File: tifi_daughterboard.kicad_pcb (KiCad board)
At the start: 2 copper layers, 57.4 x 32.3 mm, 26 parts, among them J1 SSW-110-23-F-D, J2 SSW-110-23-F-D, J3 SM04B-SRSS-TB(LF)(SN), J4 SSW-103-02-T-S-RA, J5 PH2-04-UA, Q1 BSS138LT1G, U1 SGP40-D-R4, U2 SHT40-AD1B-R3

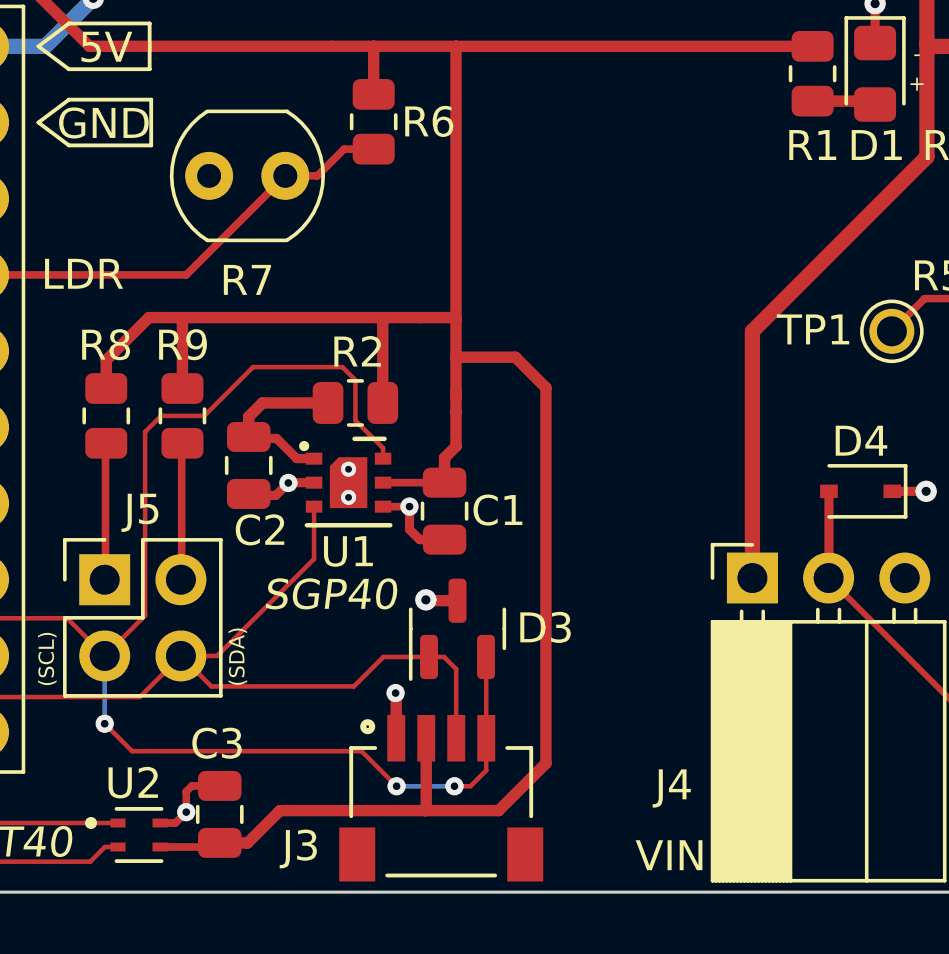
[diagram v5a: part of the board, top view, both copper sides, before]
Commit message: Add bulk capacitors to schmatic and board.
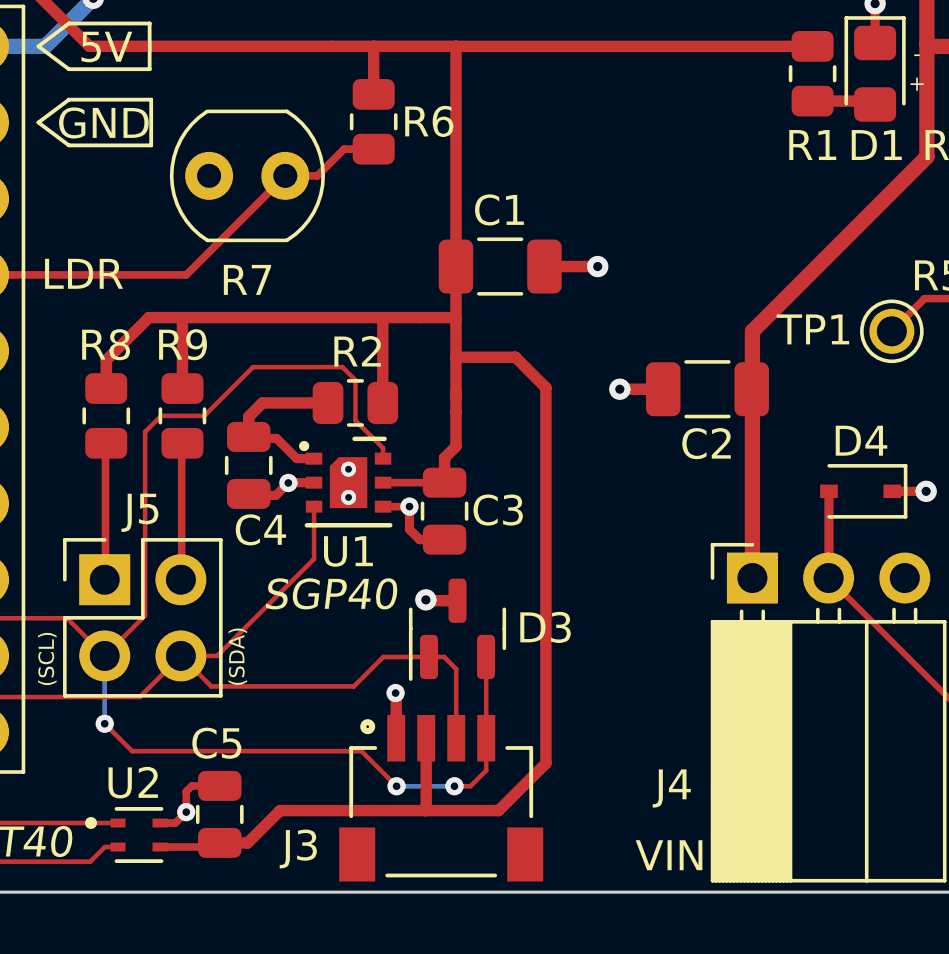
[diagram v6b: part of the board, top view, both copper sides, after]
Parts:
- added C1: 22uF, Capacitor_SMD:C_1206_3216Metric, F.Cu at (141.7, 81.0)
- added C2: 22uF, Capacitor_SMD:C_1206_3216Metric, F.Cu at (148.6, 85.1)
- renumbered C1 to C3, C2 to C4, C3 to C5
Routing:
- net GND: track 15.6 -> 18.8 mm, vias 11 -> 13
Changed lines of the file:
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@@
   (net 41 "unconnected-(J2-Pad20)")
   (net 42 "Net-(Q1-Pad2)")
-  (net 43 "Net-(C2-Pad1)")
+  (net 43 "Net-(R2-Pad2)")
   (net 44 "unconnected-(J1-Pad9)")
   (net 45 "Net-(J5-Pad1)")
@@
       (net 1 "+3.3V") (pintype "passive"))
     (pad "2" smd roundrect (at 0.9125 0 180) (size 1.025 1.4) (layers "F.Cu" "F.Paste" "F.Mask") (roundrect_rratio 0.243902439)
-      (net 43 "Net-(C2-Pad1)") (pintype "passive"))
+      (net 43 "Net-(R2-Pad2)") (pintype "passive"))
     (model "${KICAD6_3DMODEL_DIR}/Resistor_SMD.3dshapes/R_0805_2012Metric.wrl"
       (offset (xyz 0 0 0))
@@
     (property "Sheetname" "")
     (attr smd)
-    (fp_text reference "C2" (at 2.1844 -0.4064 180) (layer "F.SilkS")
+    (fp_text reference "C4" (at 2.1844 -0.4064 180) (layer "F.SilkS")
       (effects (font (size 1 1) (thickness 0.15)))
     )
@@
     (fp_line (start -1 0.625) (end -1 -0.625) (layer "F.Fab") (width 0.1))
     (pad "1" smd roundrect (at -0.95 0 270) (size 1 1.45) (layers "F.Cu" "F.Paste" "F.Mask") (roundrect_rratio 0.25)
-      (net 43 "Net-(C2-Pad1)") (pintype "passive"))
+      (net 43 "Net-(R2-Pad2)") (pintype "passive"))
     (pad "2" smd roundrect (at 0.95 0 270) (size 1 1.45) (layers "F.Cu" "F.Paste" "F.Mask") (roundrect_rratio 0.25)
       (net 2 "GND") (pintype "passive"))
@@
     )
   )
+  (footprint "Capacitor_SMD:C_1206_3216Metric" (layer "F.Cu")
+    (at 148.59 85.09 180)
+    (descr "Capacitor SMD 1206 (3216 Metric), square (rectangular) end terminal, IPC_7351 nominal, (Body size source: IPC-SM-782 page 76, https://www.pcb-3d.com/wordpress/wp-content/uploads/ipc-sm-782a_amendment_1_and_2.pdf), generated with kicad-footprint-generator")
+    (tags "capacitor")
+    (property "Sheetfile" "tifi_daughterboard.kicad_sch")
+    (property "Sheetname" "")
+    (property "Supplier Link" "https://www.digikey.com/en/products/detail/samsung-electro-mechanics/CL31B226MPHNNNE/3888806")
+    (attr smd)
+    (fp_text reference "C2" (at 0 -1.85) (layer "F.SilkS")
+      (effects (font (size 1 1) (thickness 0.15)))
+    )
+    (fp_text value "22uF" (at 0 1.85) (layer "F.Fab")
+      (effects (font (size 1 1) (thickness 0.15)))
+    )
+    (fp_text user "${REFERENCE}" (at 0 0) (layer "F.Fab")
+      (effects (font (size 0.8 0.8) (thickness 0.12)))
+    )
+    (fp_line (start -0.711252 0.91) (end 0.711252 0.91) (layer "F.SilkS") (width 0.12))
+    (fp_line (start -0.711252 -0.91) (end 0.711252 -0.91) (layer "F.SilkS") (width 0.12))
+    (fp_line (start -2.3 1.15) (end -2.3 -1.15) (layer "F.CrtYd") (width 0.05))
+    (fp_line (start 2.3 1.15) (end -2.3 1.15) (layer "F.CrtYd") (width 0.05))
+    (fp_line (start 2.3 -1.15) (end 2.3 1.15) (layer "F.CrtYd") (width 0.05))
+    (fp_line (start -2.3 -1.15) (end 2.3 -1.15) (layer "F.CrtYd") (width 0.05))
+    (fp_line (start 1.6 -0.8) (end 1.6 0.8) (layer "F.Fab") (width 0.1))
+    (fp_line (start -1.6 0.8) (end -1.6 -0.8) (layer "F.Fab") (width 0.1))
+    (fp_line (start -1.6 -0.8) (end 1.6 -0.8) (layer "F.Fab") (width 0.1))
+    (fp_line (start 1.6 0.8) (end -1.6 0.8) (layer "F.Fab") (width 0.1))
+    (pad "1" smd roundrect (at -1.475 0 180) (size 1.15 1.8) (layers "F.Cu" "F.Paste" "F.Mask") (roundrect_rratio 0.217391)
+      (net 6 "+5V") (pintype "passive"))
+    (pad "2" smd roundrect (at 1.475 0 180) (size 1.15 1.8) (layers "F.Cu" "F.Paste" "F.Mask") (roundrect_rratio 0.217391)
+      (net 2 "GND") (pintype "passive"))
+    (model "${KICAD6_3DMODEL_DIR}/Capacitor_SMD.3dshapes/C_1206_3216Metric.wrl"
+      (offset (xyz 0 0 0))
+      (scale (xyz 1 1 1))
+      (rotate (xyz 0 0 0))
+    )
+  )
   (footprint "LED_SMD:LED_0805_2012Metric_Pad1.15x1.40mm_HandSolder" (layer "F.Cu")
     (at 160.2486 74.5654 -90)
@@
     (property "Sheetfile" "tifi_daughterboard.kicad_sch")
     (property "Sheetname" "")
+    (property "Supplier Link" "https://www.digikey.com/en/products/detail/onsemi/BSS138LT1G/918376")
     (attr smd)
     (fp_text reference "Q1" (at 0 -2.7178 180) (layer "F.SilkS")
@@
     (property "Sheetname" "")
     (attr smd)
-    (fp_text reference "C3" (at 2.3368 -0.0762 180) (layer "F.SilkS")
+    (fp_text reference "C5" (at 2.3368 -0.0762 180) (layer "F.SilkS")
       (effects (font (size 1 1) (thickness 0.15)))
     )
@@
       (chamfer_ratio 0.24) (chamfer top_left))
     (pad "1" smd rect (at -1.15 -0.8) (size 0.55 0.4) (layers "F.Cu" "F.Paste" "F.Mask")
-      (net 43 "Net-(C2-Pad1)") (pinfunction "VDD") (pintype "power_in"))
+      (net 43 "Net-(R2-Pad2)") (pinfunction "VDD") (pintype "power_in"))
     (pad "2" smd rect (at -1.15 0) (size 0.55 0.4) (layers "F.Cu" "F.Paste" "F.Mask")
       (net 2 "GND") (pinfunction "VSS") (pintype "power_in"))
@@
       (net 12 "PIR_OUT") (pinfunction "A2") (pintype "passive"))
     (model "${KICAD6_3DMODEL_DIR}/Diode_SMD.3dshapes/D_SOD-323F.wrl"
+      (offset (xyz 0 0 0))
+      (scale (xyz 1 1 1))
+      (rotate (xyz 0 0 0))
+    )
+  )
+  (footprint "Capacitor_SMD:C_1206_3216Metric" (layer "F.Cu")
+    (at 141.6812 81.0006)
+    (descr "Capacitor SMD 1206 (3216 Metric), square (rectangular) end terminal, IPC_7351 nominal, (Body size source: IPC-SM-782 page 76, https://www.pcb-3d.com/wordpress/wp-content/uploads/ipc-sm-782a_amendment_1_and_2.pdf), generated with kicad-footprint-generator")
+    (tags "capacitor")
+    (property "Sheetfile" "tifi_daughterboard.kicad_sch")
+    (property "Sheetname" "")
+    (property "Supplier Link" "https://www.digikey.com/en/products/detail/samsung-electro-mechanics/CL31A226MQHNNNE/3887429")
+    (attr smd)
+    (fp_text reference "C1" (at 0 -1.85) (layer "F.SilkS")
+      (effects (font (size 1 1) (thickness 0.15)))
+    )
+    (fp_text value "22uF" (at 0 1.85) (layer "F.Fab")
+      (effects (font (size 1 1) (thickness 0.15)))
+    )
+    (fp_text user "${REFERENCE}" (at 0 0) (layer "F.Fab")
+      (effects (font (size 0.8 0.8) (thickness 0.12)))
+    )
+    (fp_line (start -0.711252 0.91) (end 0.711252 0.91) (layer "F.SilkS") (width 0.12))
+    (fp_line (start -0.711252 -0.91) (end 0.711252 -0.91) (layer "F.SilkS") (width 0.12))
+    (fp_line (start 2.3 -1.15) (end 2.3 1.15) (layer "F.CrtYd") (width 0.05))
+    (fp_line (start -2.3 1.15) (end -2.3 -1.15) (layer "F.CrtYd") (width 0.05))
+    (fp_line (start -2.3 -1.15) (end 2.3 -1.15) (layer "F.CrtYd") (width 0.05))
+    (fp_line (start 2.3 1.15) (end -2.3 1.15) (layer "F.CrtYd") (width 0.05))
+    (fp_line (start 1.6 -0.8) (end 1.6 0.8) (layer "F.Fab") (width 0.1))
+    (fp_line (start 1.6 0.8) (end -1.6 0.8) (layer "F.Fab") (width 0.1))
+    (fp_line (start -1.6 0.8) (end -1.6 -0.8) (layer "F.Fab") (width 0.1))
+    (fp_line (start -1.6 -0.8) (end 1.6 -0.8) (layer "F.Fab") (width 0.1))
+    (pad "1" smd roundrect (at -1.475 0) (size 1.15 1.8) (layers "F.Cu" "F.Paste" "F.Mask") (roundrect_rratio 0.217391)
+      (net 1 "+3.3V") (pintype "passive"))
+    (pad "2" smd roundrect (at 1.475 0) (size 1.15 1.8) (layers "F.Cu" "F.Paste" "F.Mask") (roundrect_rratio 0.217391)
+      (net 2 "GND") (pintype "passive"))
+    (model "${KICAD6_3DMODEL_DIR}/Capacitor_SMD.3dshapes/C_1206_3216Metric.wrl"
       (offset (xyz 0 0 0))
       (scale (xyz 1 1 1))
@@
     (property "Sheetfile" "tifi_daughterboard.kicad_sch")
     (property "Sheetname" "")
-    (attr exclude_from_pos_files)
+    (property "exclude_from_bom" "")
+    (attr exclude_from_pos_files exclude_from_bom)
     (fp_text reference "TP1" (at -2.5654 -0.0254) (layer "F.SilkS")
       (effects (font (size 1 1) (thickness 0.15)))
@@
     (property "Sheetname" "")
     (attr smd)
-    (fp_text reference "C1" (at 0 -1.8034 180) (layer "F.SilkS")
+    (fp_text reference "C3" (at 0 -1.8034 180) (layer "F.SilkS")
       (effects (font (size 1 1) (thickness 0.15)))
     )
@@
   (segment (start 131.2164 99.187) (end 130.8544 99.549) (width 0.254) (layer "F.Cu") (net 2))
   (segment (start 159.258 78.7654) (end 159.258 79.9908) (width 0.381) (layer "F.Cu") (net 2))
+  (segment (start 143.1562 81.0006) (end 144.9324 81.0006) (width 0.381) (layer "F.Cu") (net 2))
   (segment (start 157.9626 85.2678) (end 157.9626 83.8943) (width 0.3048) (layer "F.Cu") (net 2))
   (segment (start 135.4766 88.204) (end 134.6302 88.204) (width 0.3048) (layer "F.Cu") (net 2))
   (segment (start 138.999 90.104) (end 139.827 90.104) (width 0.3048) (layer "F.Cu") (net 2))
   (segment (start 131.4044 98.3132) (end 131.2164 98.5012) (width 0.254) (layer "F.Cu") (net 2))
+  (segment (start 147.115 85.09) (end 145.669 85.09) (width 0.381) (layer "F.Cu") (net 2))
   (segment (start 134.2034 88.6308) (end 134.62 88.2142) (width 0.3048) (layer "F.Cu") (net 2))
   (segment (start 154.178 72.2376) (end 154.178 73.549) (width 0.3048) (layer "F.Cu") (net 2))
   (segment (start 138.6586 89.0016) (end 138.6586 89.7636) (width 0.3048) (layer "F.Cu") (net 2))
   (segment (start 133.2992 88.6308) (end 134.2034 88.6308) (width 0.3048) (layer "F.Cu") (net 2))
+  (via (at 144.9324 81.0006) (size 0.7112) (drill 0.3048) (layers "F.Cu" "B.Cu") (free) (net 2))
   (via (at 131.2164 99.187) (size 0.6096) (drill 0.254) (layers "F.Cu" "B.Cu") (free) (net 2))
   (via (at 154.178 72.2376) (size 0.7112) (drill 0.3048) (layers "F.Cu" "B.Cu") (free) (net 2))
@@
   (via (at 138.6586 89.0016) (size 0.6096) (drill 0.254) (layers "F.Cu" "B.Cu") (net 2))
   (via (at 136.6266 87.757) (size 0.508) (drill 0.2286) (layers "F.Cu" "B.Cu") (free) (net 2))
+  (via (at 145.669 85.09) (size 0.7112) (drill 0.3048) (layers "F.Cu" "B.Cu") (free) (net 2))
   (via (at 159.258 78.7654) (size 0.7112) (drill 0.3048) (layers "F.Cu" "B.Cu") (free) (net 2))
   (via (at 134.62 88.2142) (size 0.6096) (drill 0.254) (layers "F.Cu" "B.Cu") (free) (net 2))
